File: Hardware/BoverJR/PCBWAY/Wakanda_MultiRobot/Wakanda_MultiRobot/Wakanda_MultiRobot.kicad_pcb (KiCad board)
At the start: 2 copper layers, 50 x 50 mm, 34 parts, among them J1 Alimentacion, J10 I2C, J11 M1, J12 M2, J3 Sensor Distancia 1, J4 Conn_01X03, J5 Conn_01X03, J6 Conn_01X03, J7 TATAMI Frontal Derecho, J8 TATAMI Frontal Izquierdo, J9 Programador, P1 Mounting_Hole, P2 Mounting_Hole, P3 Mounting_Hole, P4 Mounting_Hole, SW1 START, U1 ESP32-WROOM-32E, U2 TB67H451AFNG, U3 DRV8872, U4 AP2112K-3.3

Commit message: casi termino PCB
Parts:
- removed R1, R2: Risen, EESTN5:PTC_1210
- U3: value DRV8872 -> TB67H451AFNG
- moved J7 41.5 mm to (185.8, 62.5), turned to 180 degrees
- moved C7 6.50 mm to (162.0, 84.5)
- moved U3 3.91 mm to (163.0, 93.5)
- moved C2 3.31 mm to (159.0, 95.5)
- moved J3 3.00 mm to (146.5, 76.0)
- moved J4 3.00 mm to (146.5, 79.0)
- moved J5 1.44 mm to (185.6, 65.5)
- moved C3 1.41 mm to (153.0, 91.5)
- moved C8 1.21 mm to (153.5, 62.5)
- moved R3 1.10 mm to (152.5, 66.0)
- moved C5 1.06 mm to (143.0, 63.2)
- moved C6 1.00 mm to (151.0, 62.5), turned to -90 degrees
- moved U4 0.91 mm to (146.5, 63.2)
- moved J6 0.50 mm to (185.6, 68.5)
- moved J9 0.25 mm to (184.2, 74.5)
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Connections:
- J1 pad 1: +BATT -> Vin
- SW1 pad 2: +3V3 -> +5V
- U1 pad 10: /START -> unconnected-(U1-IO34-Pad10)
- U1 pad 11: /TATAMI_FI -> /START
- U1 pad 12: /TATAMI_FD -> /TATAMI_FI
- U1 pad 15: /M_DER_B -> /M_IZQ_B
- U1 pad 16: /M_DER_A -> /M_IZQ_A
- U1 pad 25: /M_IZQ_A -> /M_DER_B
- U1 pad 27: /M_IZQ_B -> /M_DER_A
- U1 pad 36: unconnected-(U1-IO23-Pad36) -> /TATAMI_FD
- U2 pad 4: unconnected-(U2-VREF-Pad4) -> +5V
- U2 pad 7: Net-(U2-RS) -> GND
- U3 pad 4: unconnected-(U3-nFAULT-Pad4) -> +5V
- U3 pad 7: Net-(U3-ISEN) -> GND
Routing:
- net +5V: track 0.00 -> 170.2 mm
- net Vin: track 0.00 -> 38.2 mm
- net /SCL: track 0.00 -> 32.3 mm
- net /M_DER_A: track 0.00 -> 29.6 mm
- net /EN: track 0.00 -> 29.1 mm
- net Net-(U3-OUT2): track 0.00 -> 28.8 mm
- net /M_DER_B: track 0.00 -> 27.1 mm
- net Net-(U3-OUT1): track 0.00 -> 26.4 mm
- net /M_IZQ_B: track 0.00 -> 23.0 mm
- net /M_IZQ_A: track 0.00 -> 20.6 mm
- net /SDA: track 0.00 -> 15.6 mm
- net /TXD: track 0.00 -> 14.9 mm
- net +3V3: track 0.00 -> 13.4 mm
- net /SENSOR2: track 0.00 -> 13.2 mm
- net Net-(U2-OUT1): track 0.00 -> 12.6 mm
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- added copper zone on B.Cu, net GND
- added copper zone on F.Cu, net GND

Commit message: placa casi terminada falta 3d y estetica
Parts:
- moved LOGO1 59.0 mm to (182.8, 93.5)
- moved R4 1.35 mm to (170.8, 82.8)
- moved J12 0.78 mm to (184.7, 106.2), turned to 0 degrees
- moved J11 0.76 mm to (145.2, 106.2), turned to 0 degrees
- moved C7 0.25 mm to (162.2, 84.5)
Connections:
- J11 pad 1: Net-(U2-OUT2) -> Net-(U2-OUT1)
- J11 pad 2: Net-(U2-OUT1) -> Net-(U2-OUT2)
- J12 pad 1: Net-(U3-OUT2) -> Net-(U3-OUT1)
- J12 pad 2: Net-(U3-OUT1) -> Net-(U3-OUT2)
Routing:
- net +3V3: track 13.4 -> 51.2 mm
- net /SENSOR3: track 0.00 -> 15.4 mm, vias 0 -> 1
- net /SENSOR4: track 0.00 -> 13.1 mm, vias 0 -> 1
- net GND: track 5.81 -> 2.81 mm
- net /M_DER_B: track 27.1 -> 29.0 mm
- net /M_DER_A: track 29.6 -> 31.2 mm
- net /M_IZQ_B: track 23.0 -> 21.8 mm
- net /SENSOR2: track 13.2 -> 12.3 mm
- net /IO0: track 7.01 -> 7.78 mm
- net /EN: track 29.1 -> 29.8 mm
- net +5V: track 170.2 -> 170.8 mm

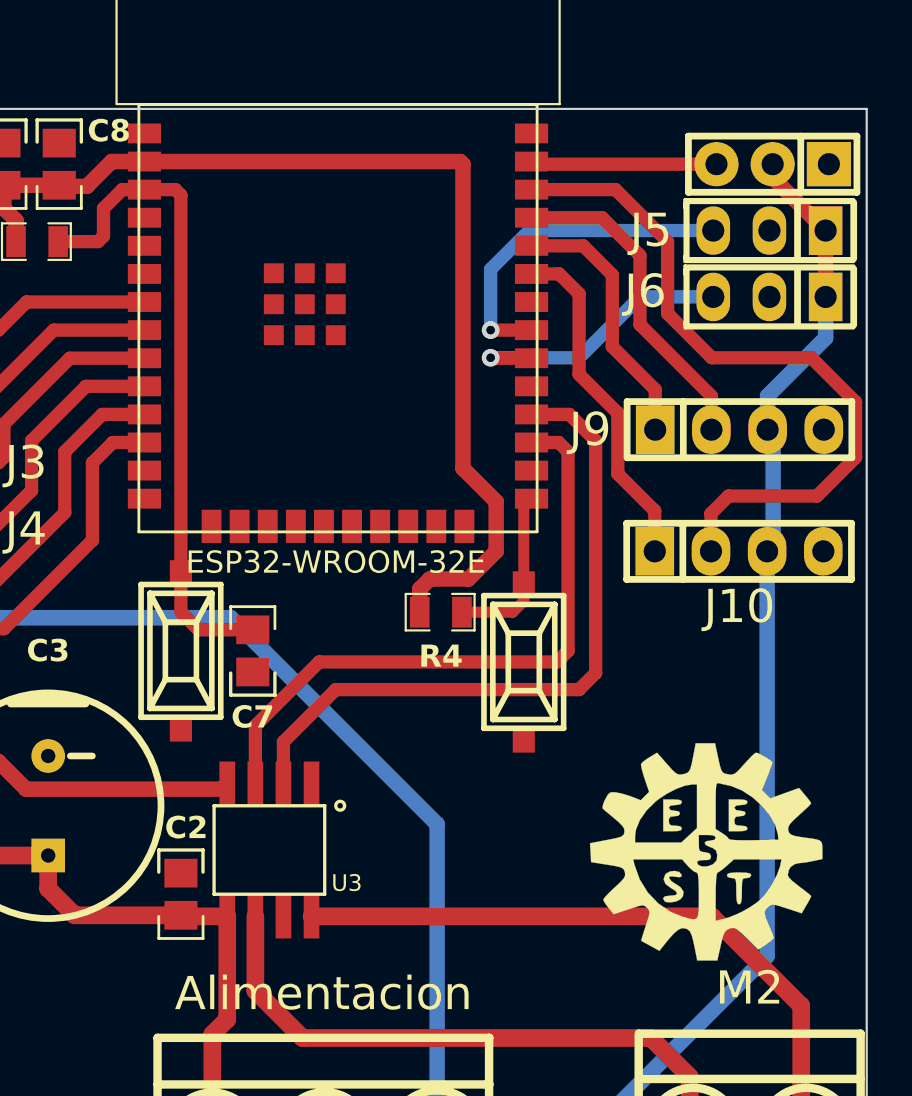
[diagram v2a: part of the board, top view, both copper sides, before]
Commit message: AÑADI BOTON A LABERINTO CHASIS PLACA
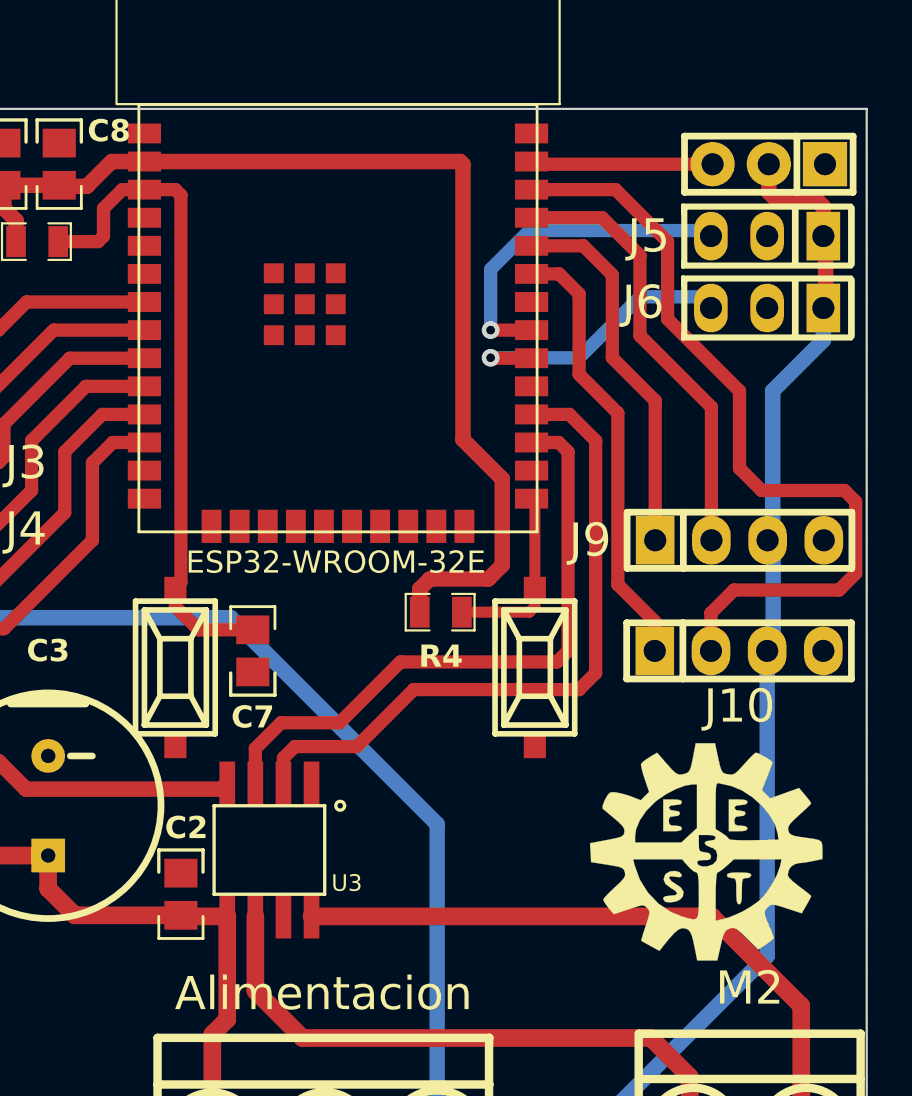
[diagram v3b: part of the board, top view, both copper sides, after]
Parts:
- moved J9 5.00 mm to (184.2, 79.5)
- moved J10 4.50 mm to (184.2, 84.5)
- moved EN1 0.79 mm to (158.8, 85.2)
- moved BOOT1 0.56 mm to (175.0, 85.2)
- moved J6 0.51 mm to (185.5, 69.0)
- moved J5 0.27 mm to (185.5, 65.8)
- moved J7 0.18 mm to (185.6, 62.5)
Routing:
- net /RXD: track 12.0 -> 17.0 mm
- net /TXD: track 14.8 -> 19.8 mm
- net /SDA: track 15.6 -> 20.1 mm
- net /SCL: track 32.3 -> 36.8 mm
- net +5V: track 170.8 -> 171.9 mm
- net +3V3: track 51.2 -> 52.0 mm
- net /M_DER_B: track 29.0 -> 28.4 mm
- net /IO0: track 7.78 -> 8.34 mm

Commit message: verifique por 3d
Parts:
- J7, J8: footprint EESTN5:Pin_Strip_3 -> EESTN5:Pin_Header_3
- moved J2 1.05 mm to (146.5, 80.0)
- moved J3 0.50 mm to (146.5, 76.5)
- moved SW1 0.45 mm to (146.5, 69.5)
- renumbered J4 to J2
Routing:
- net +5V: track 171.9 -> 171.3 mm
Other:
- board text added: "BATT GND +5V"

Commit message: recomendacion de bustos
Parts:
- added J14: RANDOM, EESTN5:pin_strip_4, F.Cu at (184.5, 85.5)
- added J4: Conn_01X03, EESTN5:Pin_Header_3, F.Cu at (146.7, 68.4)
- C3: footprint EESTN5:CAP_ELEC_10X8mm -> EESTN5:CAP_ELEC_5x11mm
- moved J9 5.00 mm to (184.2, 74.5)
- moved J10 4.50 mm to (184.2, 80.0)
- moved SW1 2.05 mm to (146.6, 71.6)
- moved J8 1.80 mm to (146.6, 74.8)
- moved C7 1.70 mm to (162.2, 82.8)
- moved J3 1.50 mm to (146.6, 78.0)
- moved J2 1.15 mm to (146.6, 81.2)
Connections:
- U1 pad 10: unconnected-(U1-IO34-Pad10) -> /SENSOR5
- U1 pad 24: unconnected-(U1-IO4-Pad24) -> /GPIO4
- U1 pad 34: unconnected-(U1-IO5-Pad34) -> /GPIO5
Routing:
- net /GPIO5: track 0.00 -> 21.3 mm
- net +5V: track 171.3 -> 150.9 mm, vias 0 -> 3
- net /GPIO4: track 0.00 -> 15.6 mm
- net /SENSOR5: track 0.00 -> 8.54 mm
- net /SCL: track 36.8 -> 28.3 mm, vias 0 -> 1
- net /M_DER_A: track 30.8 -> 25.7 mm, vias 0 -> 2
- net /RXD: track 17.0 -> 12.0 mm
- net /TXD: track 19.8 -> 14.8 mm
- net /SDA: track 20.1 -> 15.6 mm
- net /M_DER_B: track 28.4 -> 25.7 mm, vias 0 -> 2
- net /SENSOR2: track 12.7 -> 15.3 mm
- net /SENSOR1: track 11.4 -> 13.4 mm
- net /M_IZQ_B: track 21.8 -> 23.9 mm
- net /SENSOR3: track 15.4 -> 13.6 mm
- net /TATAMI_FI: track 9.55 -> 11.1 mm
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
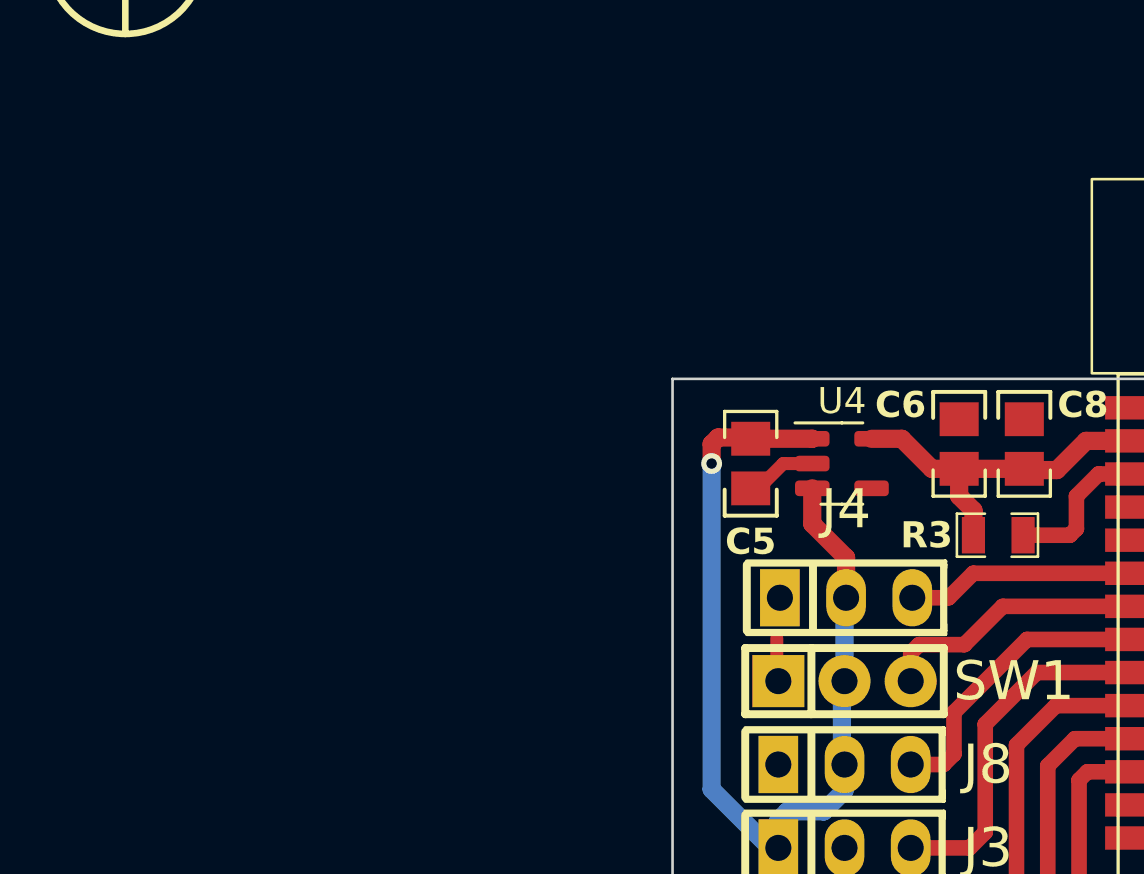
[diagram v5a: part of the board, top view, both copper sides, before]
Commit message: debo cambiar regulador ap21 3v3 por ams1117 3v3 lpm
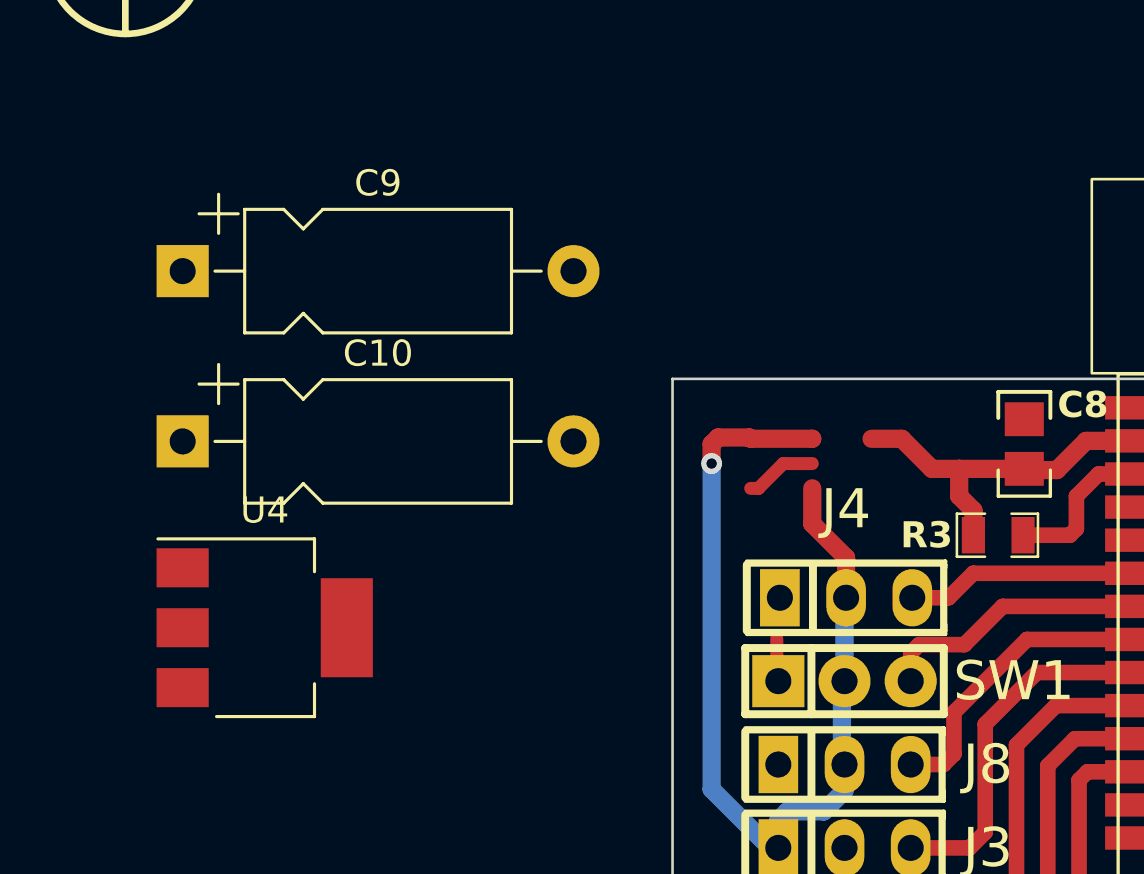
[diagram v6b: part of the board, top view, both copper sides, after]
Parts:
- removed C5, C6: 1uF, EESTN5:C_0805
- added C10: 10uF, Capacitor_THT:CP_Axial_L10.0mm_D4.5mm_P15.00mm_Horizontal, F.Cu at (121.2, 62.4)
- added C9: 100uF, Capacitor_THT:CP_Axial_L10.0mm_D4.5mm_P15.00mm_Horizontal, F.Cu at (121.2, 55.9)
- U4: value AP2112K-3.3 -> AMS1117-3.3; footprint Package_TO_SOT_SMD:SOT-23-5 -> Package_TO_SOT_SMD:SOT-223-3_TabPin2
- moved U4 23.0 mm to (124.3, 69.5)
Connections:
- U4 pad 1: +5V -> GND
- U4 pad 2: GND -> +3V3

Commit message: mejore y quedo listo para verificar wakanda multi
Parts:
- removed P1: Mounting_Hole, EESTN5:Separador_M3_5mm
- C10, C9: footprint Capacitor_THT:CP_Axial_L10.0mm_D4.5mm_P15.00mm_Horizontal -> EESTN5:CAP_ELEC_SMD_4X5.5
- LOGO1: footprint EESTN5:LOGO_EESTN5 -> EESTN5:Bover_Huella_frontal_FCU
- moved P3 91.6 mm to (186.8, 98.1)
- moved P2 76.7 mm to (152.9, 98.1)
- moved C10 68.8 mm to (182.8, 93.0), turned to -90 degrees
- moved C9 61.1 mm to (169.7, 93.0), turned to 90 degrees
- moved U4 57.6 mm to (176.2, 94.6), turned to 90 degrees
- moved LOGO1 43.6 mm to (149.8, 64.9)
- moved P4 30.8 mm to (143.0, 63.0)
- moved U2 3.10 mm to (144.6, 93.6)
- moved J4 3.00 mm to (146.6, 71.4)
- moved J2 3.00 mm to (146.6, 84.2)
- moved J3 3.00 mm to (146.6, 81.0)
- moved J8 3.00 mm to (146.6, 77.8)
- moved SW1 3.00 mm to (146.6, 74.6)
- moved R3 2.10 mm to (154.6, 66.0)
- moved C1 1.91 mm to (141.4, 100.4)
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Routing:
- net +3V3: track 51.5 -> 66.1 mm
- net /M_IZQ_B: track 23.9 -> 27.7 mm
- net /M_IZQ_A: track 21.9 -> 25.7 mm
- net /START: track 10.0 -> 13.7 mm, vias 0 -> 1
- net /TATAMI_FI: track 11.1 -> 14.5 mm
- net /SENSOR2: track 15.3 -> 18.6 mm
- net Net-(U2-OUT1): track 12.6 -> 9.47 mm
- net Net-(U2-OUT2): track 12.5 -> 9.39 mm
- net /SENSOR1: track 13.4 -> 16.4 mm
- net +5V: track 150.9 -> 148.0 mm
- net /EN: track 28.7 -> 26.7 mm
- net /SENSOR5: track 8.54 -> 9.84 mm
- net Net-(U3-OUT2): track 28.8 -> 27.5 mm
- net Vin: track 38.9 -> 37.9 mm

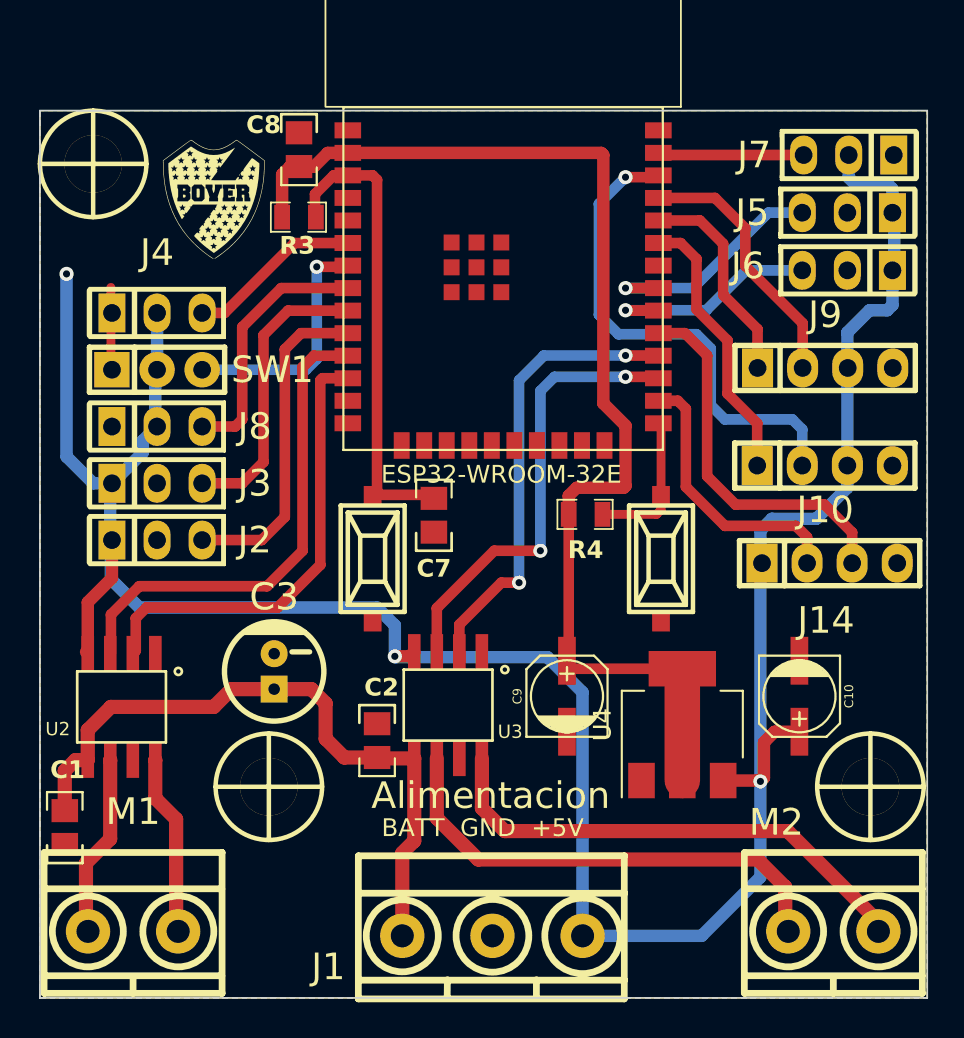
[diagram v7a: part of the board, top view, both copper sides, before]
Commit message: falta verificar por 3d
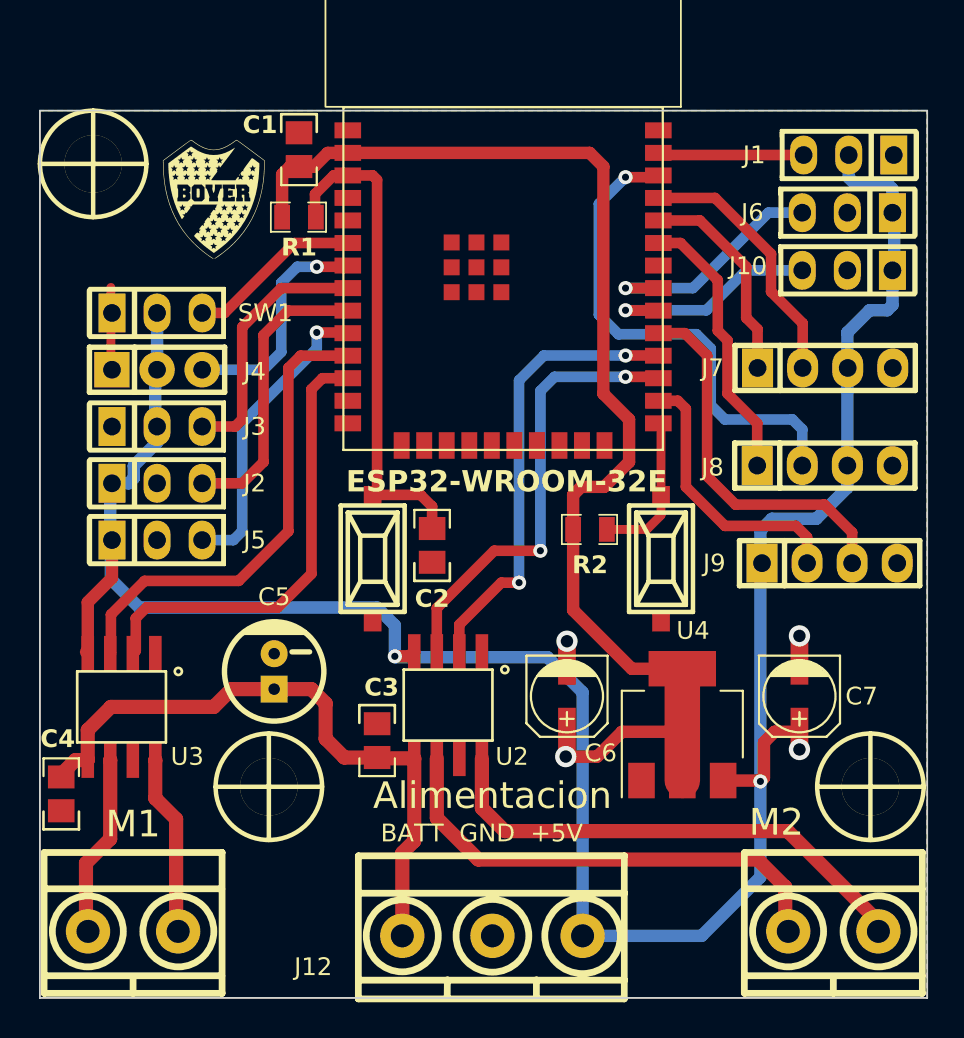
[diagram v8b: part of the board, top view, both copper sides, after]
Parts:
- moved C4 1.91 mm to (141.2, 98.5)
- moved C2 1.70 mm to (162.1, 84.5)
- moved R2 0.89 mm to (171.0, 83.6)
- turned C6 to -90 degrees
- renumbered C8 to C1, C7 to C2, C2 to C3, C1 to C4, C3 to C5, C9 to C6, C10 to C7, J7 to J1, J6 to J10, J1 to J12, J12 to J13, J3 to J2, J8 to J3, J2 to J5, J5 to J6, J9 to J7, J10 to J8, J14 to J9, P4 to P1, R3 to R1, R4 to R2, U3 to U2, U2 to U3
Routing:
- net +5V: track 148.0 -> 135.1 mm
- net +3V3: track 66.1 -> 71.5 mm, vias 0 -> 1
- net Vin: track 37.9 -> 36.1 mm
- net /SENSOR2: track 18.6 -> 17.2 mm, vias 0 -> 1
- net /EN: track 26.7 -> 28.1 mm
- net /START: track 13.7 -> 12.9 mm
- net /M_IZQ_B: track 27.7 -> 27.0 mm
- net GND: vias 0 -> 2
